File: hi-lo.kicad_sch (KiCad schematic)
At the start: 14 parts, among them U31 MIC4427, U32 MIC4427, U33 MIC4427

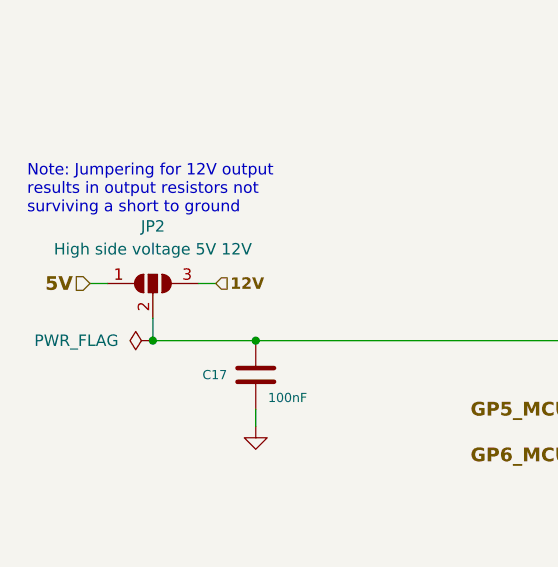
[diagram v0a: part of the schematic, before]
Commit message: replaces micro b connector by usb-c
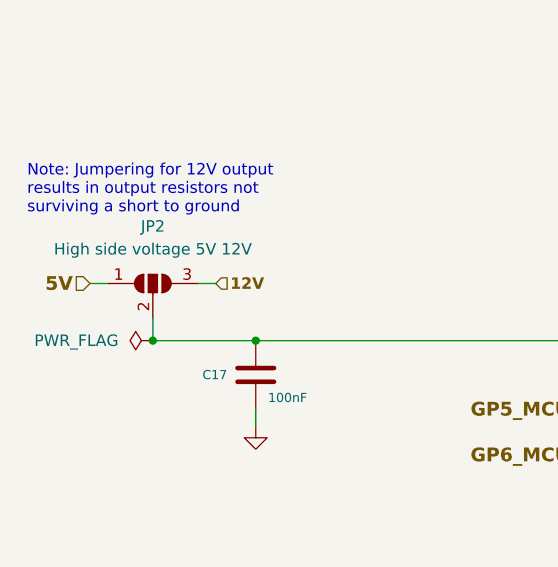
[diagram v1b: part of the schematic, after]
